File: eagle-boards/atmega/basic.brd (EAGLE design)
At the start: 59.4 x 36.8 mm, 7 parts, among them IC1 ATMEGA168-20P, Q1 BC547

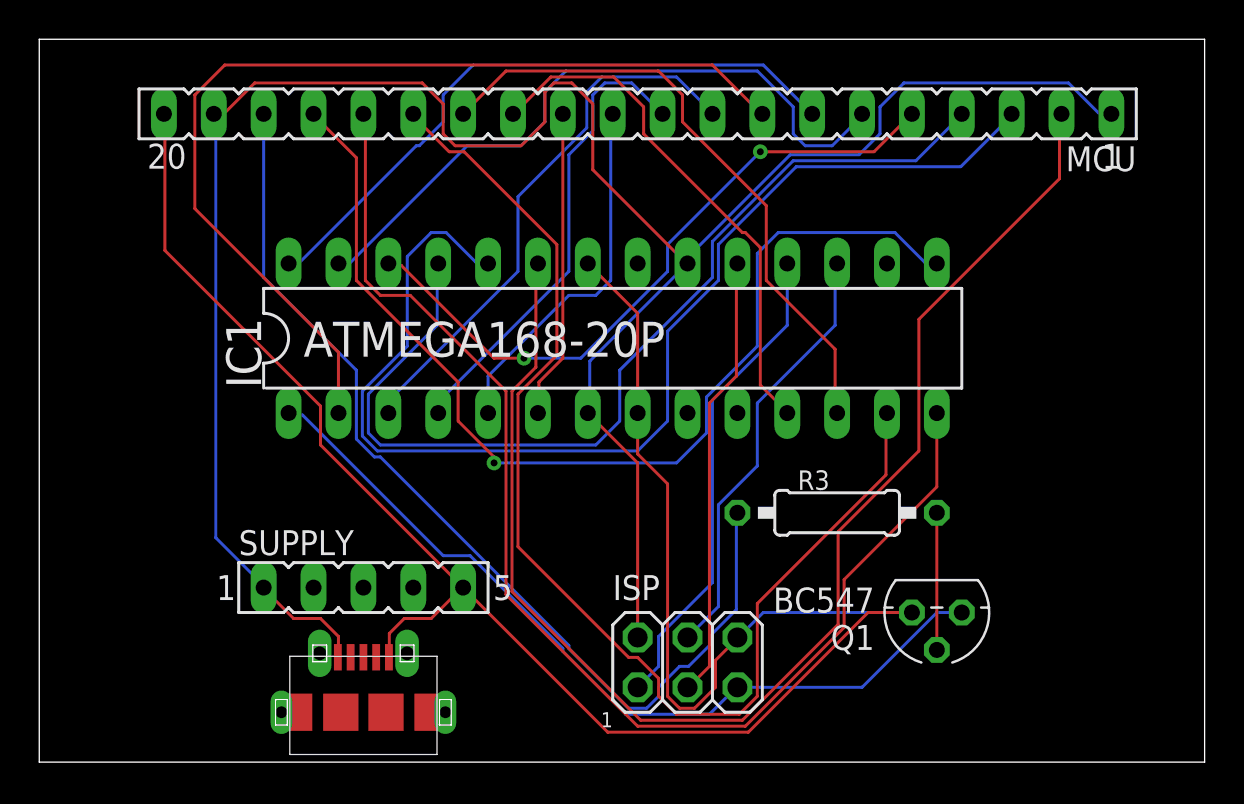
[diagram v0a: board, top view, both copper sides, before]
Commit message: Re-layout board to align with actuator.
Also update the microUSB connector to a SnapEDA symbol for an Amphenol connector that appears to be easier to source and solder.
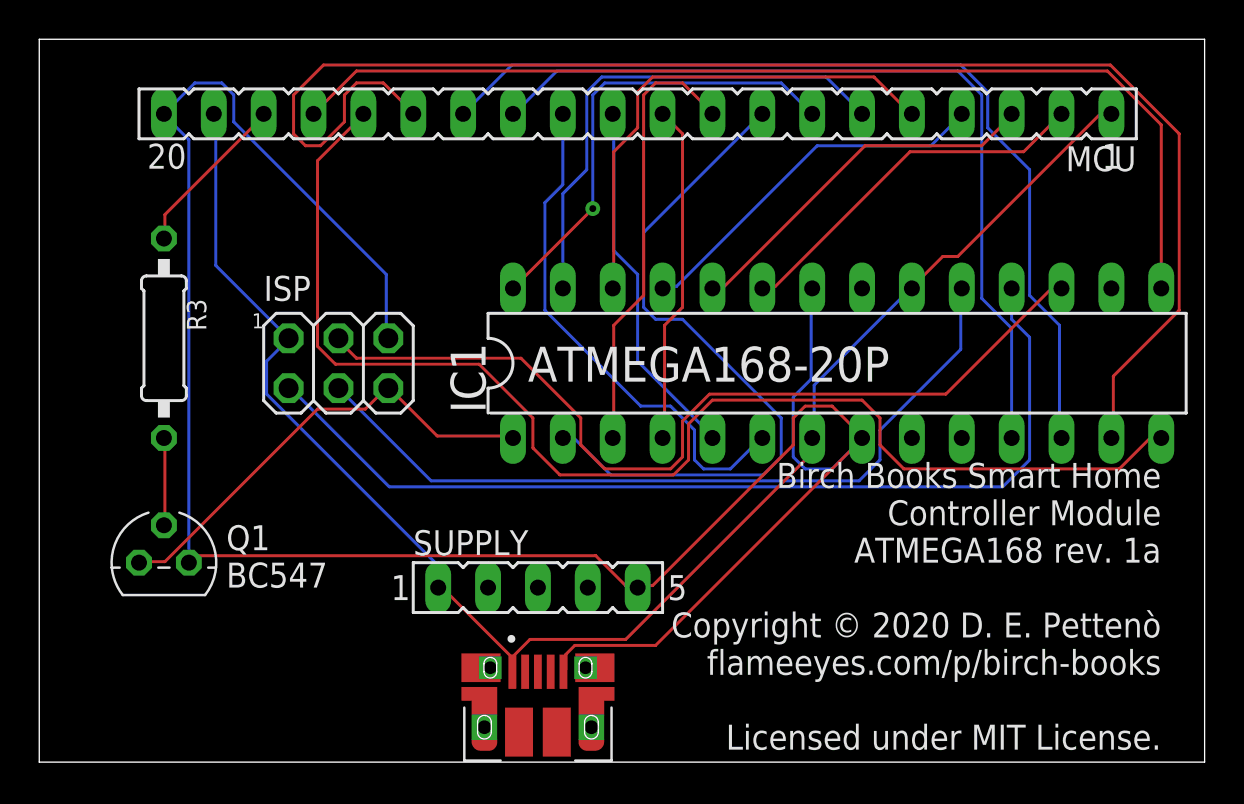
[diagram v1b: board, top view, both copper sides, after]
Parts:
- U$1: value MICRO-USB-RECEPTACLE47589-0001 -> 10103594-0001LF; device con-molex-usb:47589-0001 -> 10103594-0001LF:FCI_10103594-0001LF
- moved Q1 39.5 mm to (6.35, 10.2), turned to 0 degrees
- moved R3 35.4 mm to (6.35, 21.6), turned to 270 degrees
- moved ISP 23.4 mm to (15.2, 20.3)
- moved IC1 11.5 mm to (40.6, 20.3)
- moved U$1 8.92 mm to (25.4, 1.78), turned to 0 degrees
- moved SUPPLY 8.89 mm to (25.4, 8.89)
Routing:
- net N$5: track 69.3 -> 18.9 mm
- net N$2: track 51.2 -> 8.48 mm
- net N$6: track 59.7 -> 19.0 mm
- net +5V: track 115.4 -> 80.5 mm
- net N$7: track 50.2 -> 18.9 mm
- net N$3: track 24.7 -> 49.5 mm
- net N$1: track 22.2 -> 45.3 mm
- net N$19: track 42.9 -> 23.8 mm
- net N$4: track 22.7 -> 40.4 mm
- net N$16: track 26.8 -> 43.4 mm
- net N$18: track 32.1 -> 47.5 mm
- net N$20: track 60.1 -> 75.3 mm
- net GND: track 104.1 -> 118.1 mm
- net N$11: track 49.8 -> 36.0 mm
- net N$15: track 15.8 -> 26.3 mm
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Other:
- board text added: "Birch Books Smart Home Controller Module ATMEGA168 rev. 1a Copyright © 2020 D. E. Pettenò flameeyes.com/p/birch-books Licensed under MIT License."
- board text removed: "Birch Books Smart Home Controller Module ATMEGA168 rev. 1"
- board text removed: "Copyright © 2020 Diego Elio Pettenò flameeyes.com/p/birch-books Licensed under MIT License."
